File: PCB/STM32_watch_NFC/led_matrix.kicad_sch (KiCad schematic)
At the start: 0 parts

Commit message: Kicad - new Routing 1
Led matrix sheet added
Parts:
- added C12, C13, C14, C15, C16, C17, C18, C19, C20, C21, C22, C23: 100n, Capacitor_SMD:C_0201_0603Metric, symbol Device:C
- added D1, D10, D11, D12, D2, D3, D4, D5, D6, D7, D8, D9: SK6805, LED_SMD:LED_SK6812_EC15_1.5x1.5mm, symbol LED:SK6805
- added R6: 510, Resistor_SMD:R_0402_1005Metric, symbol Device:R
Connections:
- new net: D6.1 (DOUT), D8.3 (DIN)
- new net: D4.1 (DOUT), D6.3 (DIN)
- new net: D1.1 (DOUT), D3.3 (DIN)
- new net: D1.3 (DIN), D12.1 (DOUT)
- new net: D10.3 (DIN), D8.1 (DOUT)
- new net: D11.3 (DIN), D9.1 (DOUT)
- new net: D7.1 (DOUT), D9.3 (DIN)
- new net: D10.1 (DOUT), D12.3 (DIN)
- new net: D5.1 (DOUT), D7.3 (DIN)
- new net: D3.1 (DOUT), D5.3 (DIN)
- new net: D2.1 (DOUT), D4.3 (DIN)
- new net: D2.3 (DIN), R6.2
- new net +5V: C12.1, C13.1, C14.1, C15.1, C16.1, C17.1, C18.1, C19.1, C20.1, C21.1, C22.1, C23.1, D1.4 (VDD), D10.4 (VDD), D11.4 (VDD), D12.4 (VDD), D2.4 (VDD), D3.4 (VDD), D4.4 (VDD), D5.4 (VDD), D6.4 (VDD), D7.4 (VDD), D8.4 (VDD), D9.4 (VDD)
- new net DIN_LED: R6.1
- new net GND: C12.2, C13.2, C14.2, C15.2, C16.2, C17.2, C18.2, C19.2, C20.2, C21.2, C22.2, C23.2, D1.2 (VSS), D10.2 (VSS), D11.2 (VSS), D12.2 (VSS), D2.2 (VSS), D3.2 (VSS), D4.2 (VSS), D5.2 (VSS), D6.2 (VSS), D7.2 (VSS), D8.2 (VSS), D9.2 (VSS)
- no-connect marks 0 -> 1

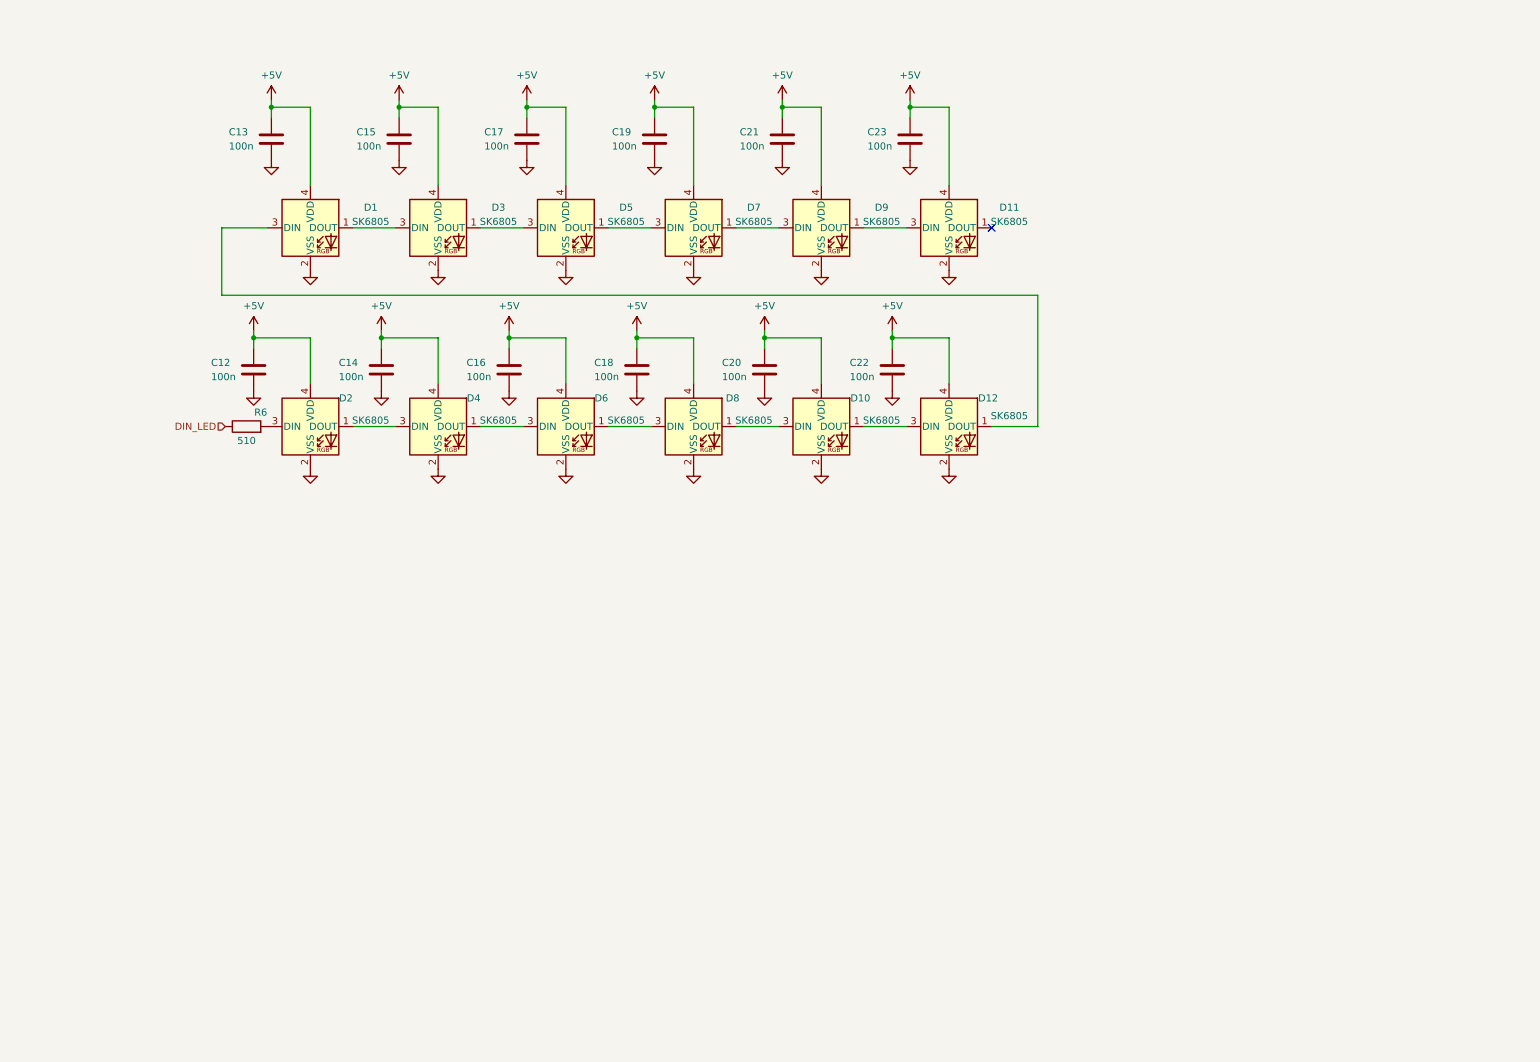
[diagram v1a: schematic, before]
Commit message: Kicad - new Routing 2
4 7-segment RGB displays for time - pretty crazy I would say
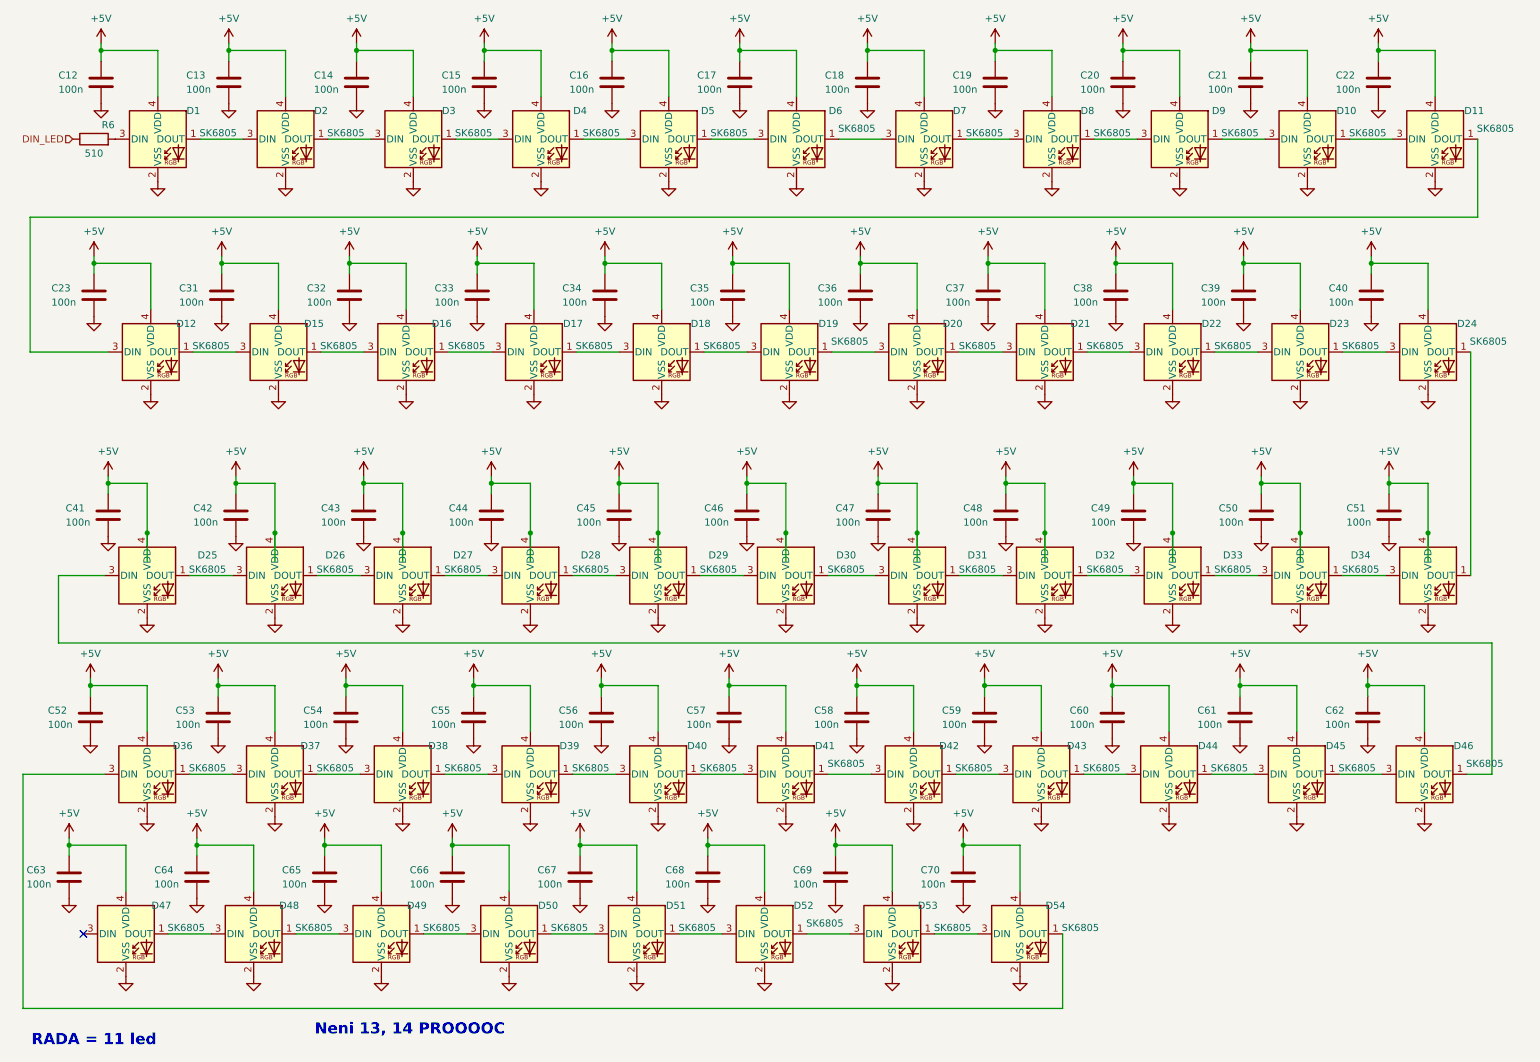
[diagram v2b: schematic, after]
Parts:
- added C12, C13, C14, C15, C16, C17, C18, C19, C20, C21, C22, C23, C31, C32, C33, C34, C35, C36, C37, C38, C39, C40, C47, C48, C49, C50, C51, C58, C59, C60, C61, C62, C63, C64, C65, C66, C67, C68, C69, C70: 100n, Capacitor_SMD:C_0201_0603Metric, symbol Device:C
- added D1, D10, D11, D12, D15, D16, D17, D18, D19, D2, D20, D21, D22, D23, D24, D3, D31, D32, D33, D34, D35, D4, D42, D43, D44, D45, D46, D47, D48, D49, D5, D50, D51, D52, D53, D54, D6, D7, D8, D9: SK6805, LED_SMD:LED_SK6812_EC15_1.5x1.5mm, symbol LED:SK6805
- renumbered C13 to C41, C15 to C42, C17 to C43, C19 to C44, C21 to C45, C23 to C46, C12 to C52, C14 to C53, C16 to C54, C18 to C55, C20 to C56, C22 to C57, D1 to D25, D3 to D26, D5 to D27, D7 to D28, D9 to D29, D11 to D30, D2 to D36, D4 to D37, D6 to D38, D8 to D39, D10 to D40, D12 to D41
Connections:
- net +5V: now also C12.1, C13.1, C14.1, C15.1, C16.1, C17.1, C18.1, C19.1, C20.1, C21.1, C22.1, C23.1, C31.1, C32.1, C33.1, C34.1, C35.1, C36.1, C37.1, C38.1, C39.1, C40.1, C47.1, C48.1, C49.1, C50.1, C51.1, C58.1, C59.1, C60.1, C61.1, C62.1, C63.1, C64.1, C65.1, C66.1, C67.1, C68.1, C69.1, C70.1, D1.4 (VDD), D10.4 (VDD), D11.4 (VDD), D12.4 (VDD), D15.4 (VDD), D16.4 (VDD), D17.4 (VDD), D18.4 (VDD), D19.4 (VDD), D2.4 (VDD), D20.4 (VDD), D21.4 (VDD), D22.4 (VDD), D23.4 (VDD), D24.4 (VDD), D3.4 (VDD), D31.4 (VDD), D32.4 (VDD), D33.4 (VDD), D34.4 (VDD), D35.4 (VDD), D4.4 (VDD), D42.4 (VDD), D43.4 (VDD), D44.4 (VDD), D45.4 (VDD), D46.4 (VDD), D47.4 (VDD), D48.4 (VDD), D49.4 (VDD), D5.4 (VDD), D50.4 (VDD), D51.4 (VDD), D52.4 (VDD), D53.4 (VDD), D54.4 (VDD), D6.4 (VDD), D7.4 (VDD), D8.4 (VDD), D9.4 (VDD)
- net GND: now also C12.2, C13.2, C14.2, C15.2, C16.2, C17.2, C18.2, C19.2, C20.2, C21.2, C22.2, C23.2, C31.2, C32.2, C33.2, C34.2, C35.2, C36.2, C37.2, C38.2, C39.2, C40.2, C47.2, C48.2, C49.2, C50.2, C51.2, C58.2, C59.2, C60.2, C61.2, C62.2, C63.2, C64.2, C65.2, C66.2, C67.2, C68.2, C69.2, C70.2, D1.2 (VSS), D10.2 (VSS), D11.2 (VSS), D12.2 (VSS), D15.2 (VSS), D16.2 (VSS), D17.2 (VSS), D18.2 (VSS), D19.2 (VSS), D2.2 (VSS), D20.2 (VSS), D21.2 (VSS), D22.2 (VSS), D23.2 (VSS), D24.2 (VSS), D3.2 (VSS), D31.2 (VSS), D32.2 (VSS), D33.2 (VSS), D34.2 (VSS), D35.2 (VSS), D4.2 (VSS), D42.2 (VSS), D43.2 (VSS), D44.2 (VSS), D45.2 (VSS), D46.2 (VSS), D47.2 (VSS), D48.2 (VSS), D49.2 (VSS), D5.2 (VSS), D50.2 (VSS), D51.2 (VSS), D52.2 (VSS), D53.2 (VSS), D54.2 (VSS), D6.2 (VSS), D7.2 (VSS), D8.2 (VSS), D9.2 (VSS)
- net at D25.3 (DIN): now also D46.1 (DOUT); no longer D41.1 (DOUT)
- net at D36.3 (DIN): now also D54.1 (DOUT); no longer R6.2
- net at D30.1 (DOUT): now also D31.3 (DIN)
- new net: D21.1 (DOUT), D22.3 (DIN)
- new net: D20.1 (DOUT), D21.3 (DIN)
- new net: D19.1 (DOUT), D20.3 (DIN)
- new net: D17.1 (DOUT), D18.3 (DIN)
- new net: D16.1 (DOUT), D17.3 (DIN)
- new net: D2.1 (DOUT), D3.3 (DIN)
- new net: D1.1 (DOUT), D2.3 (DIN)
- new net: D31.1 (DOUT), D32.3 (DIN)
- new net: D43.1 (DOUT), D44.3 (DIN)
- new net: D42.1 (DOUT), D43.3 (DIN)
- new net: D6.1 (DOUT), D7.3 (DIN)
- new net: D5.1 (DOUT), D6.3 (DIN)
- new net: D32.1 (DOUT), D33.3 (DIN)
- new net: D12.1 (DOUT), D15.3 (DIN)
- new net: D11.1 (DOUT), D12.3 (DIN)
- new net: D33.1 (DOUT), D34.3 (DIN)
- new net: D53.1 (DOUT), D54.3 (DIN)
- new net: D52.1 (DOUT), D53.3 (DIN)
- new net: D8.1 (DOUT), D9.3 (DIN)
- new net: D7.1 (DOUT), D8.3 (DIN)
- new net: D15.1 (DOUT), D16.3 (DIN)
- new net: D44.1 (DOUT), D45.3 (DIN)
- new net: D41.1 (DOUT), D42.3 (DIN)
- new net: D47.1 (DOUT), D48.3 (DIN)
- new net: D3.1 (DOUT), D4.3 (DIN)
- new net: D50.1 (DOUT), D51.3 (DIN)
- new net: D49.1 (DOUT), D50.3 (DIN)
- new net: D51.1 (DOUT), D52.3 (DIN)
- new net: D24.1 (DOUT), D35.1 (DOUT)
- new net: D34.1 (DOUT), D35.3 (DIN)
- new net: D48.1 (DOUT), D49.3 (DIN)
- new net: D1.3 (DIN), R6.2
- new net: D18.1 (DOUT), D19.3 (DIN)
- new net: D10.3 (DIN), D9.1 (DOUT)
- new net: D23.1 (DOUT), D24.3 (DIN)
- new net: D4.1 (DOUT), D5.3 (DIN)
- new net: D45.1 (DOUT), D46.3 (DIN)
- new net: D10.1 (DOUT), D11.3 (DIN)
- new net: D22.1 (DOUT), D23.3 (DIN)
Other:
- note added: "Neni 13, 14 PROOOOC"
- note added: "RADA = 11 led"
- moved on the sheet: C41, C42, C43, C44, C45, C46, C52, C53, C54, C55, C56, C57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

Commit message: Kicad - new Routing 3
TM1637 7-segment driver
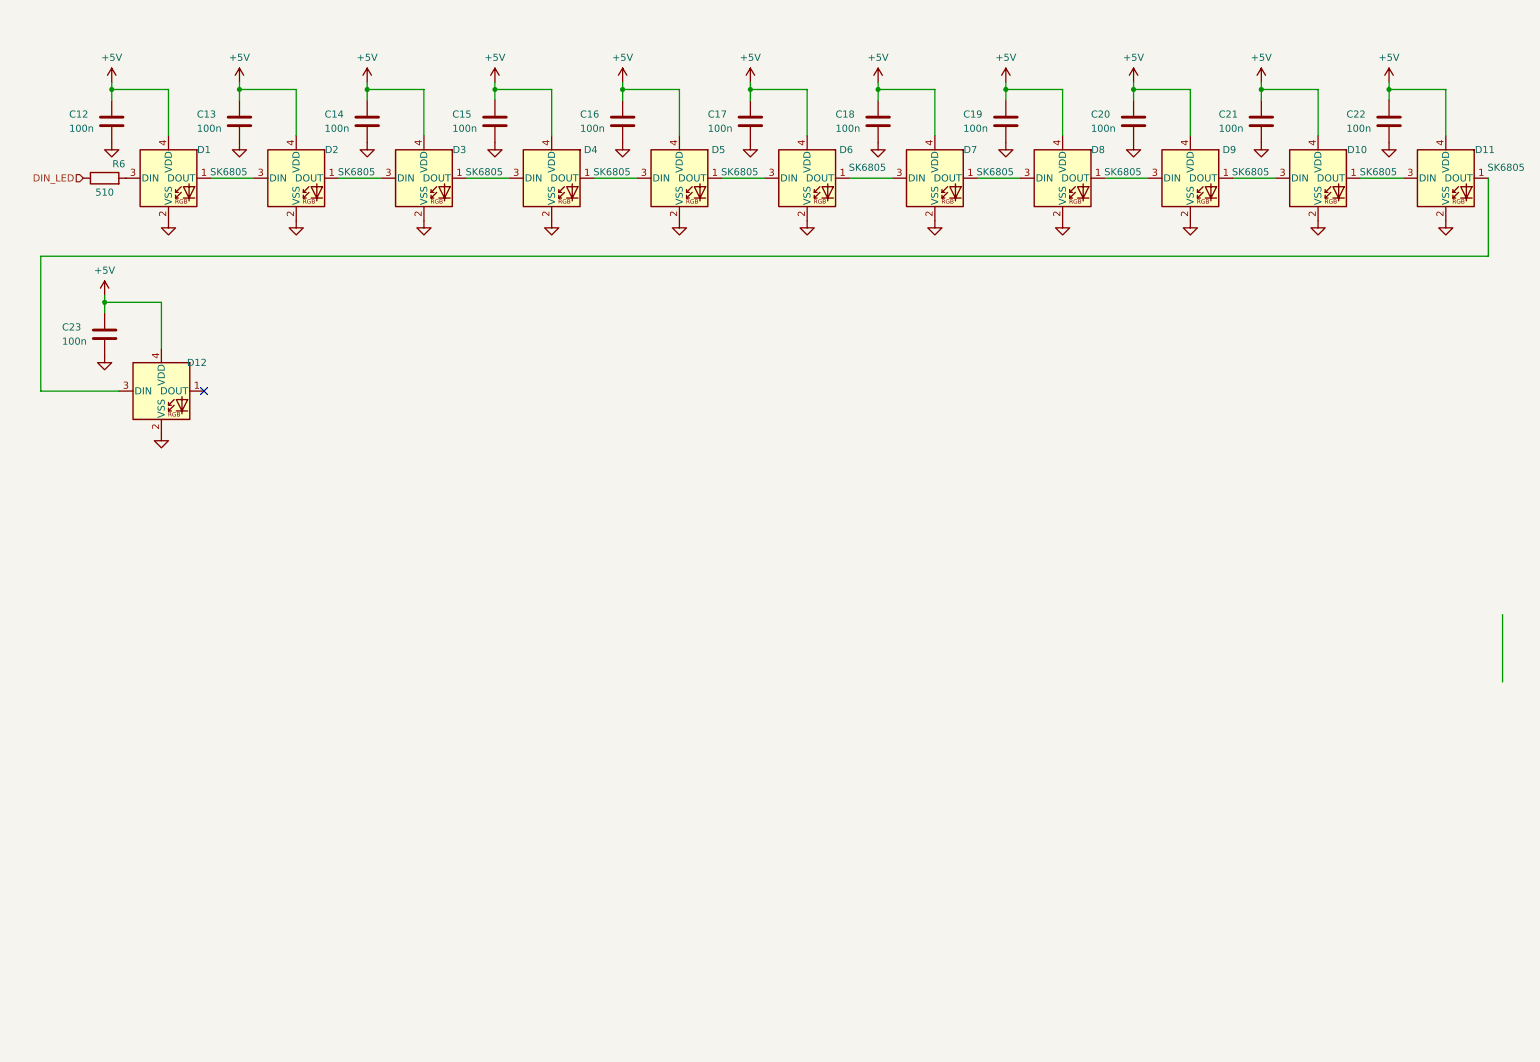
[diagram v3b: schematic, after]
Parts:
- removed C31, C32, C33, C34, C35, C36, C37, C38, C39, C40, C41, C42, C43, C44, C45, C46, C47, C48, C49, C50, C51, C52, C53, C54, C55, C56, C57, C58, C59, C60, C61, C62, C63, C64, C65, C66, C67, C68, C69, C70: 100n, Capacitor_SMD:C_0201_0603Metric, symbol Device:C
- removed D15, D16, D17, D18, D19, D20, D21, D22, D23, D24, D25, D26, D27, D28, D29, D30, D31, D32, D33, D34, D35, D36, D37, D38, D39, D40, D41, D42, D43, D44, D45, D46, D47, D48, D49, D50, D51, D52, D53, D54: SK6805, LED_SMD:LED_SK6812_EC15_1.5x1.5mm, symbol LED:SK6805
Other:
- note removed: "Neni 13, 14 PROOOOC"
- note removed: "RADA = 11 led"
- moved on the sheet: C12, C13, C14, C15, C16, C17, C18, C19, C20, C21, C22, C23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

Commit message: Kicad/STM - new Routing 6
Version before Boston to work on it there - needs to replace every component :(
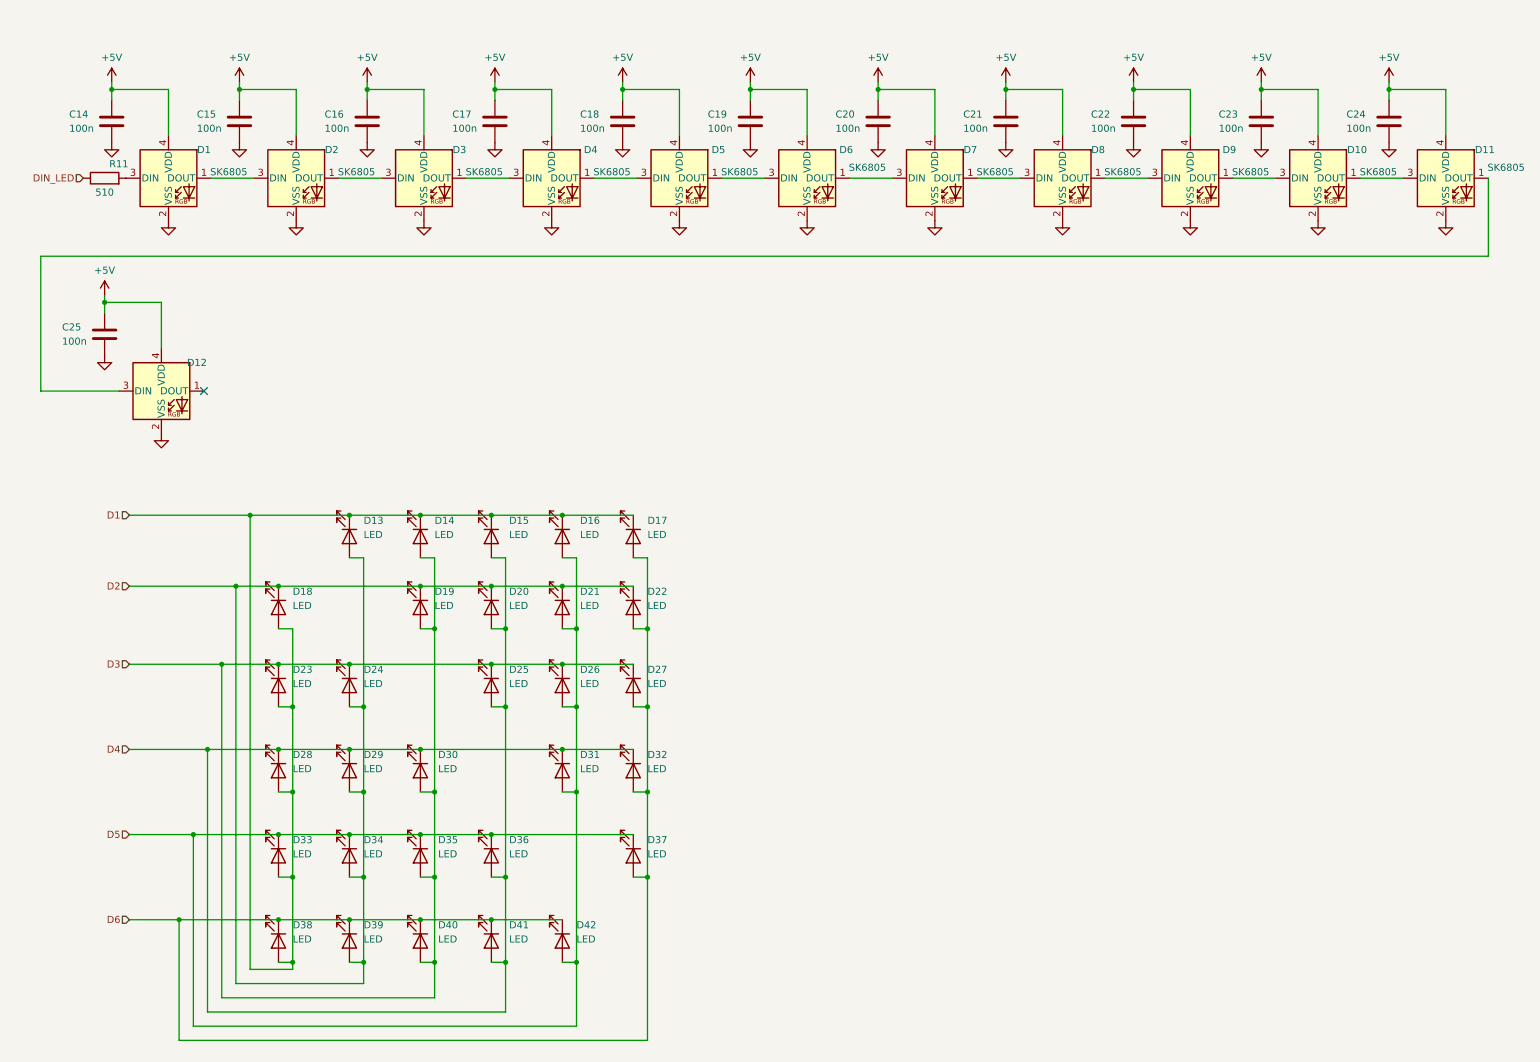
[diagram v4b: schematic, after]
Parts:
- added D13, D14, D15, D16, D17, D18, D19, D20, D21, D22, D23, D24, D25, D26, D27, D28, D29, D30, D31, D32, D33, D34, D35, D36, D37, D38, D39, D40, D41, D42: LED, LED_SMD:LED_0402_1005Metric, symbol Device:LED
- renumbered C12 to C14, C13 to C15, C14 to C16, C15 to C17, C16 to C18, C17 to C19, C18 to C20, C19 to C21, C20 to C22, C21 to C23, C22 to C24, C23 to C25, R6 to R11
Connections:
- new net D1: D13.1 (K), D14.1 (K), D15.1 (K), D16.1 (K), D17.1 (K), D18.2 (A), D23.2 (A), D28.2 (A), D33.2 (A), D38.2 (A)
- new net D2: D13.2 (A), D18.1 (K), D19.1 (K), D20.1 (K), D21.1 (K), D22.1 (K), D24.2 (A), D29.2 (A), D34.2 (A), D39.2 (A)
- new net D3: D14.2 (A), D19.2 (A), D23.1 (K), D24.1 (K), D25.1 (K), D26.1 (K), D27.1 (K), D30.2 (A), D35.2 (A), D40.2 (A)
- new net D4: D15.2 (A), D20.2 (A), D25.2 (A), D28.1 (K), D29.1 (K), D30.1 (K), D31.1 (K), D32.1 (K), D36.2 (A), D41.2 (A)
- new net D5: D16.2 (A), D21.2 (A), D26.2 (A), D31.2 (A), D33.1 (K), D34.1 (K), D35.1 (K), D36.1 (K), D37.1 (K), D42.2 (A)
- new net D6: D17.2 (A), D22.2 (A), D27.2 (A), D32.2 (A), D37.2 (A), D38.1 (K), D39.1 (K), D40.1 (K), D41.1 (K), D42.1 (K)

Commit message: Component placement
I placed every component in logical way
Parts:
- removed D41, D42: LED, LED_SMD:LED_0402_1005Metric, symbol Device:LED
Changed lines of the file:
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@@
 	)
 	(junction
-		(at 97.155 172.72)
-		(diameter 0)
-		(color 0 0 0 0)
-	)
-	(junction
 		(at 51.435 113.03)
 		(diameter 0)
@@
 	)
 	(junction
-		(at 84.455 172.72)
-		(diameter 0)
-		(color 0 0 0 0)
-	)
-	(junction
-		(at 99.695 180.34)
-		(diameter 0)
-		(color 0 0 0 0)
-	)
-	(junction
 		(at 74.295 180.34)
 		(diameter 0)
@@
 	)
 	(junction
-		(at 112.395 180.34)
-		(diameter 0)
-		(color 0 0 0 0)
-	)
-	(junction
 		(at 86.995 120.65)
 		(diameter 0)
@@
 	(wire
 		(pts
-			(xy 84.455 172.72) (xy 97.155 172.72)
-		)
-		(stroke
-			(width 0)
-			(type default)
-		)
-	)
-	(wire
-		(pts
 			(xy 125.095 149.86) (xy 122.555 149.86)
 		)
@@
 	(wire
 		(pts
-			(xy 99.695 165.1) (xy 99.695 180.34)
-		)
-		(stroke
-			(width 0)
-			(type default)
-		)
-	)
-	(wire
-		(pts
 			(xy 46.355 189.23) (xy 46.355 142.24)
 		)
@@
 	(wire
 		(pts
-			(xy 99.695 180.34) (xy 97.155 180.34)
-		)
-		(stroke
-			(width 0)
-			(type default)
-		)
-	)
-	(wire
-		(pts
 			(xy 32.385 142.24) (xy 46.355 142.24)
 		)
@@
 	(wire
 		(pts
-			(xy 112.395 180.34) (xy 112.395 191.77)
-		)
-		(stroke
-			(width 0)
-			(type default)
-		)
-	)
-	(wire
-		(pts
 			(xy 74.295 134.62) (xy 71.755 134.62)
 		)
@@
 	(wire
 		(pts
-			(xy 112.395 149.86) (xy 112.395 180.34)
+			(xy 112.395 149.86) (xy 112.395 191.77)
 		)
 		(stroke
@@
 	(wire
 		(pts
-			(xy 112.395 180.34) (xy 109.855 180.34)
-		)
-		(stroke
-			(width 0)
-			(type default)
-		)
-	)
-	(wire
-		(pts
 			(xy 53.975 100.33) (xy 71.755 100.33)
 		)
@@
 	(wire
 		(pts
-			(xy 97.155 172.72) (xy 109.855 172.72)
-		)
-		(stroke
-			(width 0)
-			(type default)
-		)
-	)
-	(wire
-		(pts
 			(xy 86.995 165.1) (xy 84.455 165.1)
 		)
@@
 	(wire
 		(pts
-			(xy 99.695 180.34) (xy 99.695 189.23)
+			(xy 99.695 165.1) (xy 99.695 189.23)
 		)
 		(stroke
@@
 	)
 	(symbol
-		(lib_id "Device:LED")
-		(at 109.855 176.53 270)
-		(unit 1)
-		(exclude_from_sim no)
-		(in_bom yes)
-		(on_board yes)
-		(dnp no)
-		(fields_autoplaced yes)
-		(property "Reference" "D42"
-			(at 112.395 173.6724 90)
-			(effects
-				(font
-					(size 1.27 1.27)
-				)
-				(justify left)
-			)
-		)
-		(property "Value" "LED"
-			(at 112.395 176.2124 90)
-			(effects
-				(font
-					(size 1.27 1.27)
-				)
-				(justify left)
-			)
-		)
-		(property "Footprint" "LED_SMD:LED_0402_1005Metric"
-			(at 109.855 176.53 0)
-			(effects
-				(font
-					(size 1.27 1.27)
-				)
-				(hide yes)
-			)
-		)
-		(property "Datasheet" "~"
-			(at 109.855 176.53 0)
-			(effects
-				(font
-					(size 1.27 1.27)
-				)
-				(hide yes)
-			)
-		)
-		(property "Description" "Light emitting diode"
-			(at 109.855 176.53 0)
-			(effects
-				(font
-					(size 1.27 1.27)
-				)
-				(hide yes)
-			)
-		)
-		(pin "2"
-		)
-		(pin "1"
-		)
-		(instances
-			(project "STM32_watch_NFC"
-				(path "/e445874f-c7a3-43dd-b930-6bce1d4fa2ef/88effd89-3120-4d43-a17e-caa30e216b86"
-					(reference "D42")
-					(unit 1)
-				)
-			)
-		)
-	)
-	(symbol
 		(lib_id "power:+5V")
 		(at 189.23 22.86 0)
@@
 					(unit 1)
 				)
-			)
-		)
-	)
-	(symbol
-		(lib_id "Device:LED")
-		(at 97.155 176.53 270)
-		(unit 1)
-		(exclude_from_sim no)
-		(in_bom yes)
-		(on_board yes)
-		(dnp no)
-		(fields_autoplaced yes)
-		(property "Reference" "D41"
-			(at 100.33 173.6724 90)
-			(effects
-				(font
-					(size 1.27 1.27)
-				)
-				(justify left)
-			)
-		)
-		(property "Value" "LED"
-			(at 100.33 176.2124 90)
-			(effects
-				(font
-					(size 1.27 1.27)
-				)
-				(justify left)
-			)
-		)
-		(property "Footprint" "LED_SMD:LED_0402_1005Metric"
-			(at 97.155 176.53 0)
-			(effects
-				(font
-					(size 1.27 1.27)
-				)
-				(hide yes)
-			)
-		)
-		(property "Datasheet" "~"
-			(at 97.155 176.53 0)
-			(effects
-				(font
-					(size 1.27 1.27)
-				)
-				(hide yes)
-			)
-		)
-		(property "Description" "Light emitting diode"
-			(at 97.155 176.53 0)
-			(effects
-				(font
-					(size 1.27 1.27)
-				)
-				(hide yes)
-			)
-		)
-		(pin "2"
-		)
-		(pin "1"
-		)
-		(instances
-			(project "STM32_watch_NFC"
-				(path "/e445874f-c7a3-43dd-b930-6bce1d4fa2ef/88effd89-3120-4d43-a17e-caa30e216b86"
-					(reference "D41")
-					(unit 1)
-				)
